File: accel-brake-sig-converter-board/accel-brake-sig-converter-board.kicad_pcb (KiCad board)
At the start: 2 copper layers, 0 parts

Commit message: 素子配置ACCEL1まで
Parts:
- added C1: 1000p, ProjectEV_Capacitor:C_3216M, F.Cu at (11.0, 5.50)
- added C10: 1u, ProjectEV_Capacitor:C_1608M, F.Cu at (-45.2, -16.1)
- added C11: 1u, ProjectEV_Capacitor:C_1608M, F.Cu at (15.0, 25.0)
- added C12: 1u, ProjectEV_Capacitor:C_1608M, F.Cu at (-41.2, -36.1)
- added C13: 1u, ProjectEV_Capacitor:C_1608M, F.Cu at (-41.2, -33.6)
- added C14: 0.1u, ProjectEV_Capacitor:C_1608M, F.Cu at (15.0, 23.2)
- added C15: 0.1u, ProjectEV_Capacitor:C_1608M, F.Cu at (-41.2, -28.6)
- added C16: 0.1u, ProjectEV_Capacitor:C_1608M, F.Cu at (-41.2, -26.1)
- added C17: 10n, ProjectEV_Capacitor:C_1608M, F.Cu at (-41.2, -23.6)
- added C18: 10n, ProjectEV_Capacitor:C_1608M, F.Cu at (-41.2, -21.1)
- added C19: 10n, ProjectEV_Capacitor:C_1608M, F.Cu at (-41.2, -18.6)
- added C2: 1u, ProjectEV_Capacitor:C_1608M, F.Cu at (22.8, 11.2)
- added C3: 1u, ProjectEV_Capacitor:C_1608M, F.Cu at (41.0, 39.6)
- added C4: 1u, ProjectEV_Capacitor:C_1608M, F.Cu at (-45.2, -31.1)
- added C5: 1u, ProjectEV_Capacitor:C_1608M, F.Cu at (21.0, 11.2)
- added C6: 1u, ProjectEV_Capacitor:C_1608M, F.Cu at (41.0, 47.1)
- added C7: 1u, ProjectEV_Capacitor:C_1608M, F.Cu at (-45.2, -23.6)
- added C8: 1u, ProjectEV_Capacitor:C_1608M, F.Cu at (16.0, 11.2)
- added C9: 1u, ProjectEV_Capacitor:C_1608M, F.Cu at (41.0, 54.6)
- added D1: PZ1AH11B-AU_R1_000A1, ProjectEV_Diode:PZ1AH11B-AU_R1_000A1, F.Cu at (20.8, 28.0)
- added D2: PZ1AH11B-AU_R1_000A1, ProjectEV_Diode:PZ1AH11B-AU_R1_000A1, F.Cu at (64.0, 41.0)
- added D3: PZ1AH11B-AU_R1_000A1, ProjectEV_Diode:PZ1AH11B-AU_R1_000A1, F.Cu at (-15.6, -53.1)
- added D4: B1911PG--20D000514U1930, ProjectEV_LED:B1911PG--20D000514U1930, F.Cu at (22.2, 31.0)
- added D5: B1911PG--20D000514U1930, ProjectEV_LED:B1911PG--20D000514U1930, F.Cu at (61.0, 48.3)
- added D6: B1911PG--20D000514U1930, ProjectEV_LED:B1911PG--20D000514U1930, F.Cu at (-25.2, -22.5)
- added D7: B1911PG--20D000514U1930, ProjectEV_LED:B1911PG--20D000514U1930, F.Cu at (13.2, 13.8)
- added D8: B1911PG--20D000514U1930, ProjectEV_LED:B1911PG--20D000514U1930, F.Cu at (61.0, 55.4)
- added D9: B1911PG--20D000514U1930, ProjectEV_LED:B1911PG--20D000514U1930, F.Cu at (-25.2, -15.5)
- added F1: 0ABB-1000-TM, ProjectEV_Fuse:0ABB-1000-TM, F.Cu at (14.0, 28.0)
- added F2: 0ABB-1000-TM, ProjectEV_Fuse:0ABB-1000-TM, F.Cu at (84.0, 27.0)
- added F3: 0ABB-1000-TM, ProjectEV_Fuse:0ABB-1000-TM, F.Cu at (14.0, 73.0)
- added H1: MountingHole_3.2mm_M3_Pad_Via, ProjectEV_Mechanical:MountingHole_3.2mm_M3_Pad_Via, F.Cu at (4.00, 4.00)
- added H2: MountingHole_3.2mm_M3_Pad_Via, ProjectEV_Mechanical:MountingHole_3.2mm_M3_Pad_Via, F.Cu at (4.00, 86.0)
- added H3: MountingHole_3.2mm_M3_Pad_Via, ProjectEV_Mechanical:MountingHole_3.2mm_M3_Pad_Via, F.Cu at (26.0, 4.00)
- added H4: MountingHole_3.2mm_M3_Pad_Via, ProjectEV_Mechanical:MountingHole_3.2mm_M3_Pad_Via, F.Cu at (26.0, 86.0)
- added J1: SM03B-PASS-TBT, ProjectEV_Connector_JST:SM03B-PASS-TBT, F.Cu at (5.00, 27.0)
- added J2: SM03B-PASS-TBT, ProjectEV_Connector_JST:SM03B-PASS-TBT, F.Cu at (5.00, 51.0)
- added J3: SM03B-PASS-TBT, ProjectEV_Connector_JST:SM03B-PASS-TBT, F.Cu at (5.00, 75.0)
- added J4: SM03B-PASS-TBT, ProjectEV_Connector_JST:SM03B-PASS-TBT, F.Cu at (5.00, 15.0)
- added J5: SM03B-PASS-TBT, ProjectEV_Connector_JST:SM03B-PASS-TBT, F.Cu at (5.00, 39.0)
- added J6: SM03B-PASS-TBT, ProjectEV_Connector_JST:SM03B-PASS-TBT, F.Cu at (5.00, 63.0)
- added Q1: DMP3098LQ-7, ProjectEV_Transistor:DMP3098LQ-7, F.Cu at (17.5, 28.0)
- added Q2: DMP3098LQ-7, ProjectEV_Transistor:DMP3098LQ-7, F.Cu at (85.0, 30.0)
- added Q3: DMP3098LQ-7, ProjectEV_Transistor:DMP3098LQ-7, F.Cu at (15.0, 76.0)
- added Q4: 2N7002K-AU_R1_000A2, ProjectEV_Transistor:2N7002K-AU_R1_000A2, F.Cu at (17.0, 14.8)
- added Q5: 2N7002K-AU_R1_000A2, ProjectEV_Transistor:2N7002K-AU_R1_000A2, F.Cu at (74.0, 47.0)
- added Q6: 2N7002K-AU_R1_000A2, ProjectEV_Transistor:2N7002K-AU_R1_000A2, F.Cu at (-12.1, -21.7)
- added R1: 1M, ProjectEV_Resistor:R_3216M, F.Cu at (11.0, 2.50)
- added R10: 100, ProjectEV_Resistor:R_1608M, F.Cu at (20.0, 14.5)
- added R11: 100, ProjectEV_Resistor:R_1608M, F.Cu at (49.0, 54.6)
- added R12: 100, ProjectEV_Resistor:R_1608M, F.Cu at (-37.1, -16.1)
- added R13: 100k, ProjectEV_Resistor:R_1608M, F.Cu at (14.2, 11.2)
- added R14: 100k, ProjectEV_Resistor:R_1608M, F.Cu at (53.0, 37.0)
- added R15: 100k, ProjectEV_Resistor:R_1608M, F.Cu at (-33.1, -33.6)
- added R16: 3.3k, ProjectEV_Resistor:R_1608M, F.Cu at (12.5, 11.2)
- added R17: 3.3k, ProjectEV_Resistor:R_1608M, F.Cu at (53.0, 44.6)
- added R18: 3.3k, ProjectEV_Resistor:R_1608M, F.Cu at (-33.1, -26.1)
- added R19: 10k, ProjectEV_Resistor:R_1608M, F.Cu at (22.0, 17.5)
- added R2: 0, ProjectEV_Resistor:R_1608M, F.Cu at (-41.2, -16.1)
- added R20: 100k, ProjectEV_Resistor:R_1608M, F.Cu at (13.2, 15.8)
- added R21: 10k, ProjectEV_Resistor:R_1608M, F.Cu at (-33.1, -18.6)
- added R22: 100k, ProjectEV_Resistor:R_1608M, F.Cu at (-33.1, -16.1)
- added R23: 10k, ProjectEV_Resistor:R_1608M, F.Cu at (-33.1, -13.6)
- added R24: 100k, ProjectEV_Resistor:R_1608M, F.Cu at (-29.1, -36.1)
- added R25: 10k, ProjectEV_Resistor:R_1608M, F.Cu at (22.0, 20.8)
- added R26: 100k, ProjectEV_Resistor:R_1608M, F.Cu at (12.5, 18.8)
- added R27: 10k, ProjectEV_Resistor:R_1608M, F.Cu at (-29.1, -28.6)
- added R28: 100k, ProjectEV_Resistor:R_1608M, F.Cu at (-29.1, -26.1)
- added R29: 10k, ProjectEV_Resistor:R_1608M, F.Cu at (-29.1, -23.6)
- added R3: 0, ProjectEV_Resistor:R_1608M, F.Cu at (-41.2, -13.6)
- added R30: 100k, ProjectEV_Resistor:R_1608M, F.Cu at (-29.1, -21.1)
- added R31: RT1206BRC07250RL, ProjectEV_Resistor:RT1206BRC07250RL, F.Cu at (20.2, 23.8)
- added R32: RT1206BRC07250RL, ProjectEV_Resistor:RT1206BRC07250RL, F.Cu at (-20.5, -11.3)
- added R33: RT1206BRC07250RL, ProjectEV_Resistor:RT1206BRC07250RL, F.Cu at (-20.5, -8.00)
- added R34: 100k, ProjectEV_Resistor:R_1608M, F.Cu at (-29.1, -18.6)
- added R35: 100k, ProjectEV_Resistor:R_1608M, F.Cu at (-29.1, -16.1)
- added R36: 100k, ProjectEV_Resistor:R_1608M, F.Cu at (-29.1, -13.6)
- added R4: 100k, ProjectEV_Resistor:R_1608M, F.Cu at (17.5, 30.8)
- added R5: 100k, ProjectEV_Resistor:R_1608M, F.Cu at (57.5, 40.8)
- added R6: 100k, ProjectEV_Resistor:R_1608M, F.Cu at (-37.1, -31.1)
- added R7: 10k, ProjectEV_Resistor:R_1608M, F.Cu at (23.0, 28.5)
- added R8: 10k, ProjectEV_Resistor:R_1608M, F.Cu at (49.0, 47.1)
- added R9: 10k, ProjectEV_Resistor:R_1608M, F.Cu at (-37.1, -23.6)
- added U1: NCV8711BMTW500TBG, ProjectEV_RegulatorLinear:NCV8711BMTW500TBG, F.Cu at (18.5, 11.2)
- added U2: NCV8711BMTW500TBG, ProjectEV_RegulatorLinear:NCV8711BMTW500TBG, F.Cu at (70.8, 59.0)
- added U3: NCV8711BMTW500TBG, ProjectEV_RegulatorLinear:NCV8711BMTW500TBG, F.Cu at (-15.3, -10.6)
- added U4: NCV20072DR2G, ProjectEV_Opamp:NCV20072DR2G, F.Cu at (17.2, 19.5)
- added U5: NCV20072DR2G, ProjectEV_Opamp:NCV20072DR2G, F.Cu at (-17.4, -33.1)
- added U6: NCV20072DR2G, ProjectEV_Opamp:NCV20072DR2G, F.Cu at (-11.0, -33.1)

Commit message: 配置およそ完了
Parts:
- moved D3 134.7 mm to (20.2, 76.8), turned to -90 degrees
- moved C13 122.2 mm to (18.5, 73.0)
- moved R6 122.2 mm to (16.8, 78.5), turned to 180 degrees
- moved R9 116.2 mm to (23.5, 75.5), turned to -90 degrees
- moved C4 114.5 mm to (24.8, 59.5), turned to -90 degrees
- moved C16 114.2 mm to (18.5, 71.2)
- moved D6 112.4 mm to (23.5, 78.8), turned to 90 degrees
- moved R24 109.9 mm to (16.8, 63.8)
- moved C7 107.5 mm to (23.0, 59.5), turned to -90 degrees
- moved R29 107.3 mm to (25.5, 68.8), turned to -90 degrees
- moved U6 105.5 mm to (20.8, 67.5), turned to 90 degrees
- moved R15 105.2 mm to (16.2, 59.2), turned to -90 degrees
- moved C12 104.0 mm to (18.5, 49.0)
- moved R12 99.4 mm to (23.5, 62.8), turned to -90 degrees
- moved C19 99.0 mm to (14.2, 63.5), turned to 90 degrees
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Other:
- board outline added: 30 x 90 mm

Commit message: 配置完了
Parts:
- moved R2 0.50 mm to (27.5, 32.5)
- moved R3 0.50 mm to (27.5, 56.5)
- moved R10 0.25 mm to (23.8, 14.8)
- moved R11 0.25 mm to (23.8, 38.8)
- moved R12 0.25 mm to (23.8, 62.8)
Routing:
- added copper zone on F.Cu, net +12V1
- added copper zone on B.Cu, net Chassis
- added copper zone on F.Cu, net Chassis
- added copper zone on B.Cu, net GND1
- added copper zone on F.Cu, net GND1
- added copper zone on B.Cu, net GND2
- added copper zone on F.Cu, net GND2
- added copper zone on B.Cu, net GND3
- added copper zone on F.Cu, net GND3
- added copper zone on F.Cu, net VCC1

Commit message: accel1配線
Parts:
- moved D7 0.25 mm to (16.8, 14.0)
- moved D8 0.25 mm to (16.8, 38.0)
- moved D9 0.25 mm to (16.8, 62.0)
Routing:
- net Net-(U4A-+): track 0.00 -> 10.0 mm
- net Net-(Q4-G): track 0.00 -> 9.61 mm
- net ACCEL1_SIG_OUT_I: track 0.00 -> 8.72 mm
- net ACCEL1_SIG_IN_V: track 0.00 -> 6.74 mm
- net Net-(D1-A): track 0.00 -> 4.90 mm
- net Net-(U4B--): track 0.00 -> 4.53 mm
- net Net-(R25-Pad2): track 0.00 -> 4.36 mm
- net Net-(U1-PG): track 0.00 -> 4.33 mm
- net Net-(U4A--): track 0.00 -> 3.69 mm
- net Net-(D7-A): track 0.00 -> 2.55 mm
- net Net-(D7-K): track 0.00 -> 2.06 mm
- net Net-(D4-A): track 0.00 -> 1.68 mm
- added copper zone on F.Cu, net Net-(J1-Pin_1)
- added copper zone on F.Cu, net Net-(Q1-D)

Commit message: 配線完了, DRC完了
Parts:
- added G***: LOGO, ProjectEV_Logo:TUT_8x7.5mm, F.Cu at (17.5, 82.5)
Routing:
- net BRAKE_SIG_OUT_I: track 0.00 -> 23.5 mm, vias 0 -> 2
- net ACCEL2_SIG_OUT_I: track 0.00 -> 23.5 mm, vias 0 -> 2
- net ACCEL1_SIG_OUT_I: track 8.72 -> 23.5 mm, vias 0 -> 2
- net Net-(U5A-+): track 0.00 -> 10.0 mm
- net Net-(U6A-+): track 0.00 -> 10.0 mm
- net Net-(Q5-G): track 0.00 -> 9.61 mm
- net Net-(Q6-G): track 0.00 -> 9.46 mm
- net BRAKE_SIG_IN_V: track 0.00 -> 6.74 mm
- net ACCEL2_SIG_IN_V: track 0.00 -> 6.74 mm
- net Net-(D2-A): track 0.00 -> 4.90 mm
- net Net-(D3-A): track 0.00 -> 4.90 mm
- net Net-(U6B--): track 0.00 -> 4.53 mm
- net Net-(U5B--): track 0.00 -> 4.53 mm
- net Net-(R29-Pad2): track 0.00 -> 4.36 mm
- net Net-(R27-Pad2): track 0.00 -> 4.36 mm
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- added copper zone on F.Cu, net +12V2
- added copper zone on F.Cu, net +12V3
- added copper zone on F.Cu, net Net-(J2-Pin_1)
- added copper zone on F.Cu, net Net-(J3-Pin_1)
- added copper zone on F.Cu, net Net-(Q2-D)
- added copper zone on F.Cu, net Net-(Q3-D)
- added copper zone on F.Cu, net VCC2
- added copper zone on F.Cu, net VCC3
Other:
- board text added: "ACCEL1"
- board text added: "ACCEL2"
- board text added: "BRAKE"
- board text added: "IOUT"
- board text added: "Project EV"
- board text added: "accel-brake-sig-converter-board-v1.0"

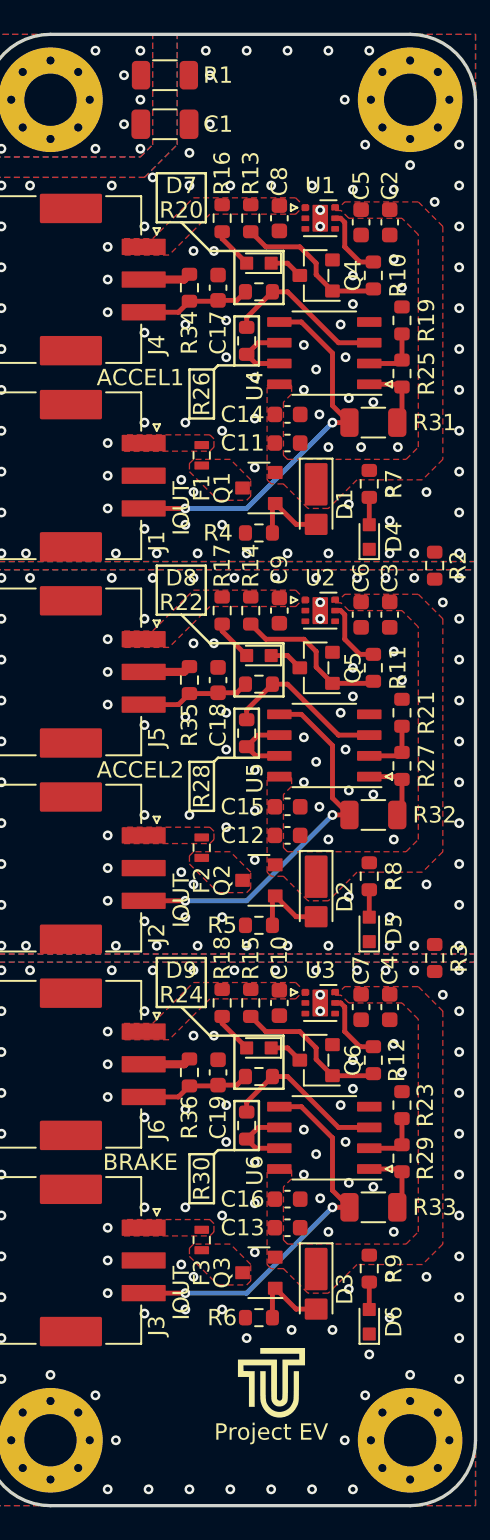
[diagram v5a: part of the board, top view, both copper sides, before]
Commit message: add fiducials, toolingholes
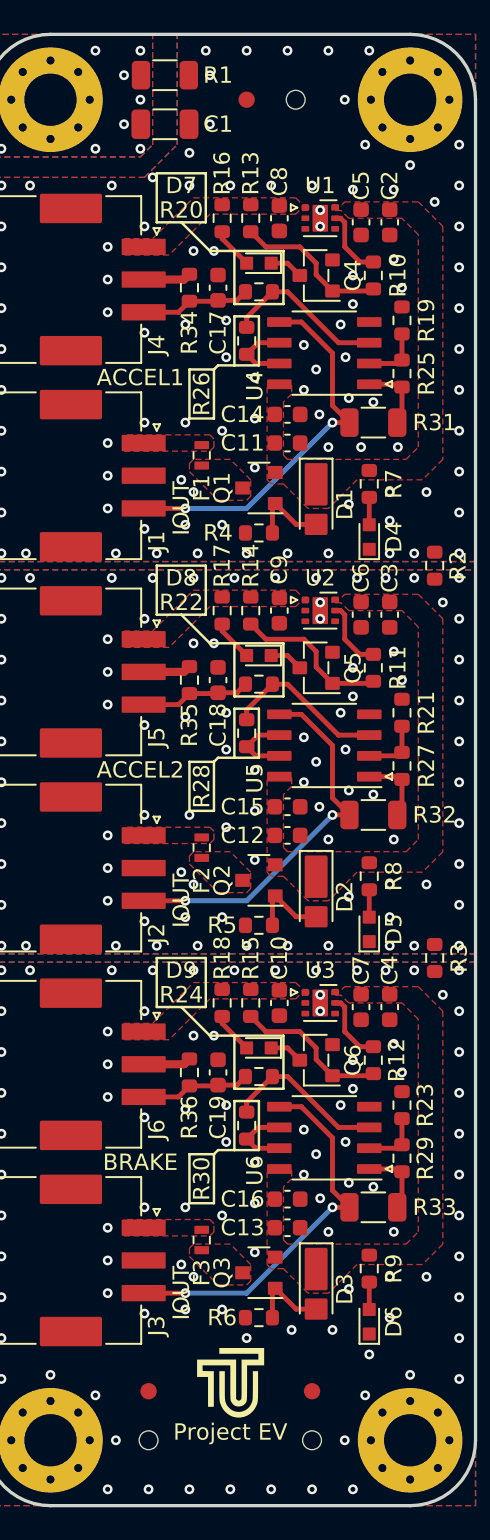
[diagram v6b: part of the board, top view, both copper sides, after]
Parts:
- added REF**: Fiducial_JLCPCB, ProjectEV_Mechanical:Fiducial_JLCPCB, F.Cu at (16.0, 4.00)
- added REF**: ToolingHole_JLCPCB, ProjectEV_Mechanical:ToolingHole_JLCPCB, F.Cu at (10.0, 86.0)
- added REF**: ToolingHole_JLCPCB, ProjectEV_Mechanical:ToolingHole_JLCPCB, F.Cu at (20.0, 86.0)
- added REF**: ToolingHole_JLCPCB, ProjectEV_Mechanical:ToolingHole_JLCPCB, F.Cu at (19.0, 4.00)
- added REF**: Fiducial_JLCPCB, ProjectEV_Mechanical:Fiducial_JLCPCB, F.Cu at (20.0, 83.0)
- added REF**: Fiducial_JLCPCB, ProjectEV_Mechanical:Fiducial_JLCPCB, F.Cu at (10.0, 83.0)
- moved G*** 2.50 mm to (15.0, 82.5)
